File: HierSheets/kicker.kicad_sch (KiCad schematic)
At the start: 0 parts

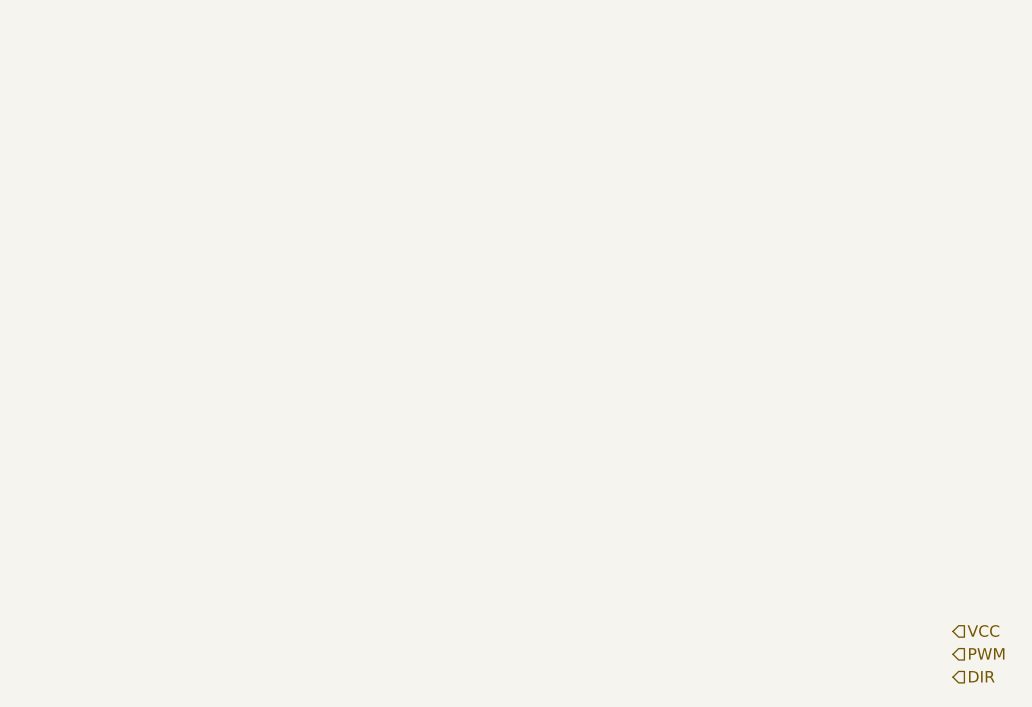
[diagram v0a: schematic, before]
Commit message: Added kicker, interrupt, I2C pullups, buck converter, button
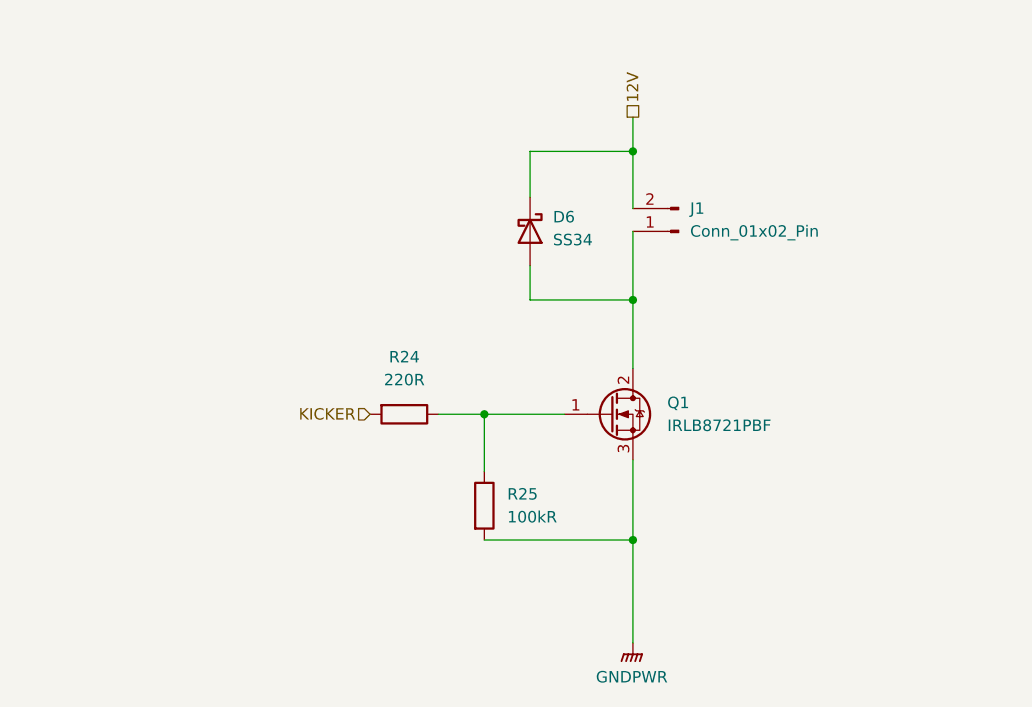
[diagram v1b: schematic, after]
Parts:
- added D6: SS34, Diode_SMD:D_SMA, symbol Diode:SS34
- added J1: Conn_01x02_Pin, symbol Connector:Conn_01x02_Pin
- added Q1: IRLB8721PBF, Package_TO_SOT_THT:TO-220-3_Vertical, symbol Transistor_FET:IRLB8721PBF
- added R24: 220R, symbol Device:R
- added R25: 100kR, symbol Device:R
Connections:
- new net: D6.2 (A), J1.1 (Pin_1), Q1.2 (D)
- new net: Q1.1 (G), R24.1, R25.1
- new net 12V: D6.1 (K), J1.2 (Pin_2)
- new net GNDPWR: Q1.3 (S), R25.2
- new net KICKER: R24.2

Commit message: Pridanie cudlika na kicker
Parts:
- added C34: 1uF, symbol Device:C
- added D17: 1N4148, Diode_THT:D_DO-35_SOD27_P7.62mm_Horizontal, symbol Diode:1N4148
- added R57: 220R, symbol Device:R
- added SW3: SW_Push, symbol Switch:SW_Push
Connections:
- net GNDPWR: now also D17.1 (K)
- net at Q1.1 (G), R24.1, R25.1: now also C34.2, D17.2 (A)
- new net: R57.1, SW3.1
- new net: C34.1, R57.2
- new net 3V3: SW3.2
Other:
- note added: "Nezabudnut nastavit ako input ked unused nedavaj nikdy LOW inak short"
- moved on the sheet: Q1
